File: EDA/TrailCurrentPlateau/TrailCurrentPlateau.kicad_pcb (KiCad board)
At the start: 2 copper layers, 56.4 x 64.2 mm, 12 parts, among them J1 DHT22, U1 Amazon Buck Converter, U2 ESP32-C6-Super-Mini, U3 SN65HVD230, U4 ZX-XH2.54-4PWT

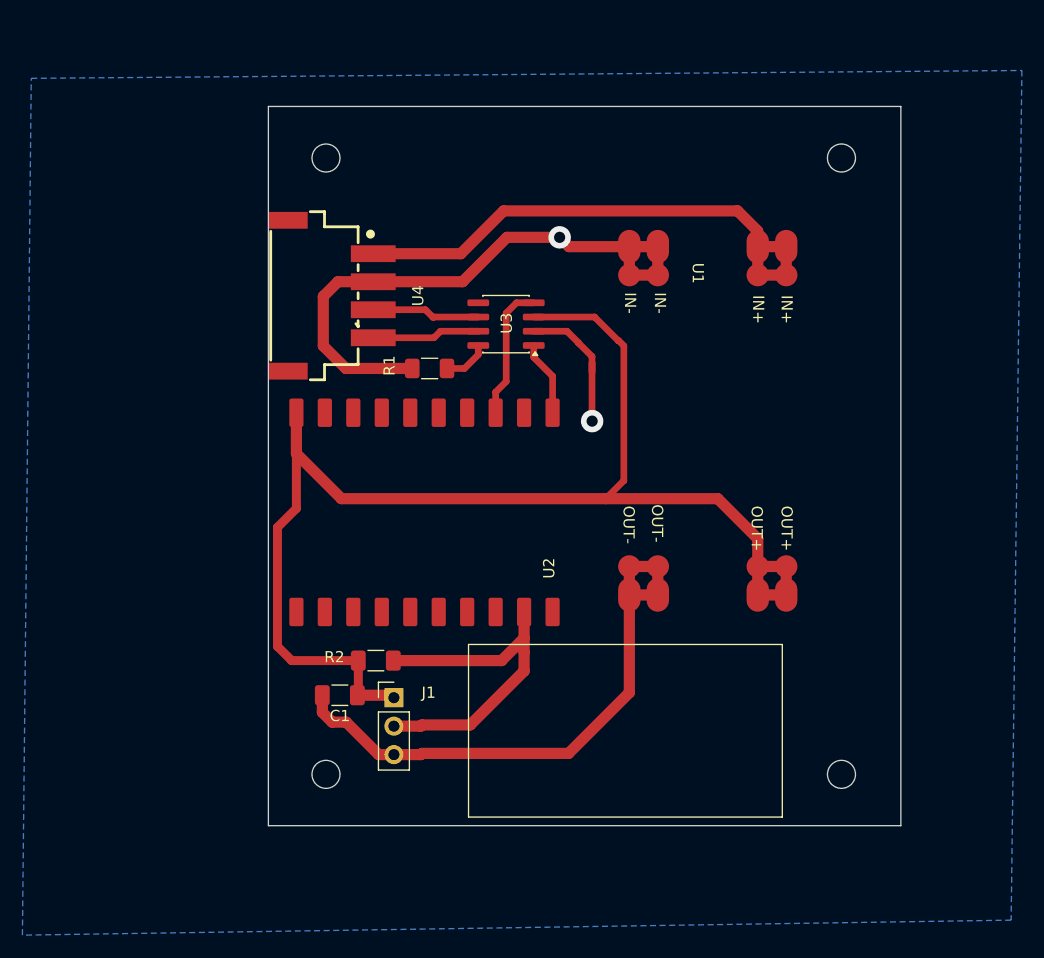
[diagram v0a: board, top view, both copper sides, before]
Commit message: Moved to ESP32S3 Zero board, adafruit bno055 and standard approach for CAN Bus and OTA
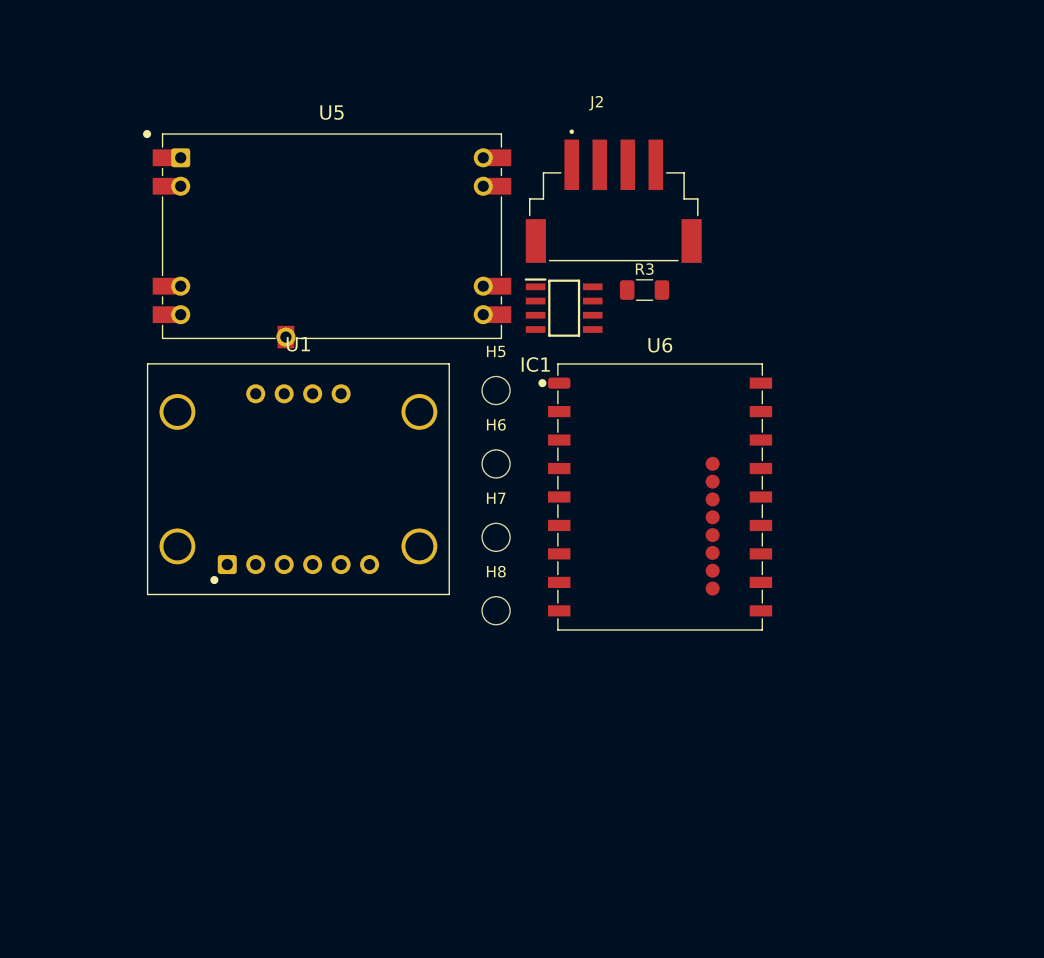
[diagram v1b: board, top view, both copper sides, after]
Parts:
- removed C1: 100nF, Capacitor_SMD:C_1206_3216Metric_Pad1.33x1.80mm_HandSolder
- removed H1, H2, H3, H4: MountingHole, MountingHole:MountingHole_2.5mm
- removed J1: DHT22, Connector_PinHeader_2.54mm:PinHeader_1x03_P2.54mm_Vertical
- removed R1: 10k, Resistor_SMD:R_1206_3216Metric_Pad1.30x1.75mm_HandSolder
- removed R2: 4.7K, Capacitor_SMD:C_1206_3216Metric_Pad1.33x1.80mm_HandSolder
- removed U2: ESP32-C6-Super-Mini, RF_Module:ESP32-C6-Super-Mini
- removed U3: SN65HVD230, Package_SO:SOIC-8_3.9x4.9mm_P1.27mm
- removed U4: ZX-XH2.54-4PWT, easyeda2kicad:CONN-SMD_4P-P2.50-WAFER-254W-4P
- added H5: MountingHole, MountingHole:MountingHole_2.5mm, F.Cu at (147.2, 85.8)
- added H6: MountingHole, MountingHole:MountingHole_2.5mm, F.Cu at (147.2, 92.3)
- added H7: MountingHole, MountingHole:MountingHole_2.5mm, F.Cu at (147.2, 98.8)
- added H8: MountingHole, MountingHole:MountingHole_2.5mm, F.Cu at (147.2, 105.4)
- added IC1: SN65HVD230DR, TrailCurrentFootprints:SN65HVD230DR, F.Cu at (153.3, 78.4)
- added J2: S4B-XH-SM4-TB, TrailCurrentFootprints:JST_S4B-XH-SM4-TB, F.Cu at (157.7, 72.4)
- added R3: 10k, Resistor_SMD:R_1206_3216Metric_Pad1.30x1.75mm_HandSolder, F.Cu at (160.4, 76.8)
- added U5: Mini560, TrailCurrentFootprints:Mini560, F.Cu at (132.5, 72.0)
- added U6: ESP32-S3-Zero, TrailCurrentFootprints:ESP32-S3-Zero_SMD, F.Cu at (161.8, 95.2)
- U1: value Amazon Buck Converter -> AdaFruit_BNO055; footprint Converter_DCDC:AmazonBuckConverter -> TrailCurrentFootprints:AdaFruit_BNO055
- moved U1 30.5 mm to (129.5, 93.7), turned to 0 degrees
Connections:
- U1 pad 1: +12V -> unconnected-(U1-VIN-Pad1)
- U1 pad 2: GND -> unconnected-(U1-3VO-Pad2)
- U1 pad 3: GND -> unconnected-(U1-GND-Pad3)
- U1 pad 4: +3.3V -> I2C_SDA
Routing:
- net GND: track 118.5 -> 0.00 mm, vias 2 -> 0
- net +3.3V: track 116.4 -> 0.00 mm
- net +12V: track 48.2 -> 0.00 mm
- net DHT_READING: track 32.7 -> 0.00 mm
- net CAN_RX: track 12.1 -> 0.00 mm
- net CANL: track 9.67 -> 0.00 mm
- net CANH: track 9.61 -> 0.00 mm
- net CAN_TX: track 6.70 -> 0.00 mm
- net Net-(U3-Rs): track 4.12 -> 0.00 mm
- removed copper zone on B.Cu, net GND
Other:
- board outline removed

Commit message: DIY EDA ready, CAM milling oeprations added
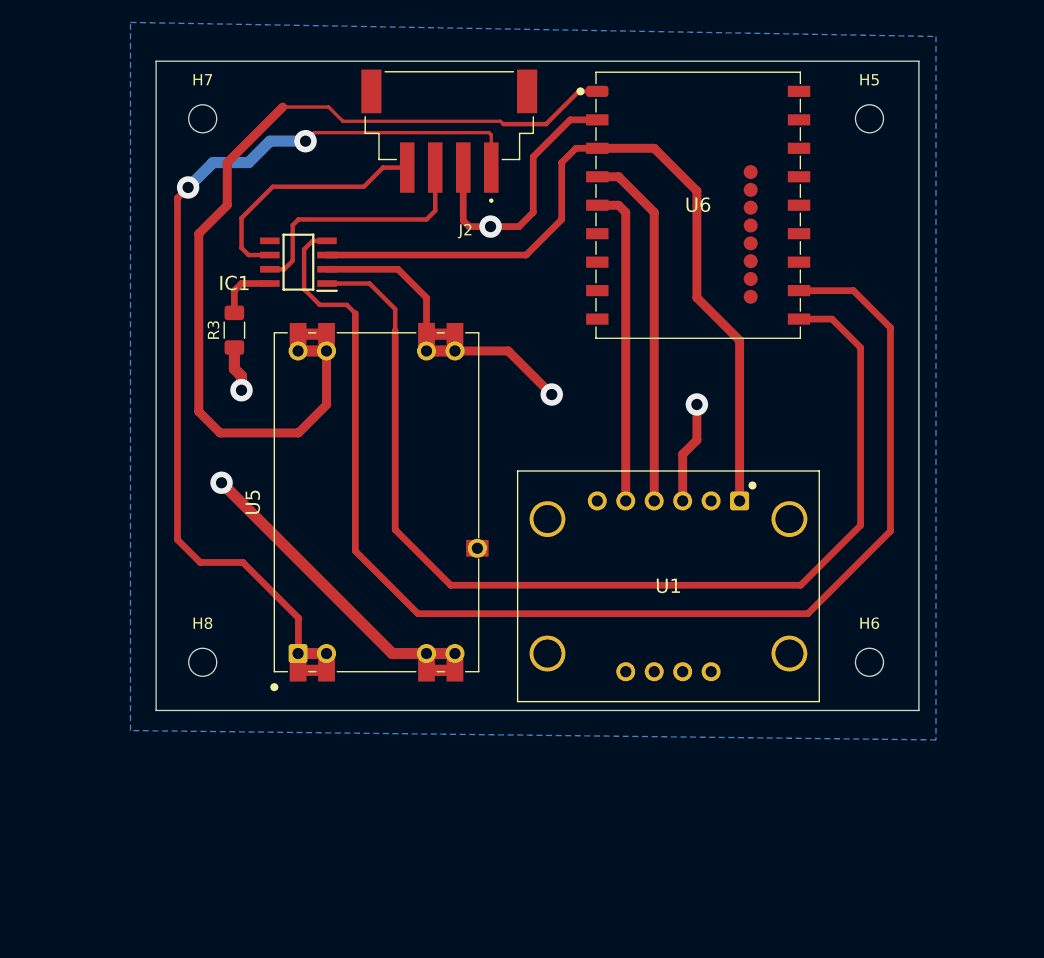
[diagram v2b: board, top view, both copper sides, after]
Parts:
- moved H7 45.6 mm to (121.0, 61.5)
- moved H5 41.2 mm to (180.5, 61.5)
- moved H6 37.7 mm to (180.5, 110.0)
- moved R3 36.8 mm to (123.8, 80.4), turned to 90 degrees
- moved U1 34.4 mm to (162.6, 103.2), turned to 180 degrees
- moved H8 26.6 mm to (121.0, 110.0)
- moved U6 26.3 mm to (165.2, 69.2)
- moved U5 24.1 mm to (136.5, 95.7), turned to 90 degrees
- moved IC1 24.1 mm to (129.5, 74.3), turned to 180 degrees
- moved J2 19.8 mm to (143.0, 59.1), turned to 180 degrees
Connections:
- U1 pad 1: unconnected-(U1-VIN-Pad1) -> +3.3V
- U1 pad 3: unconnected-(U1-GND-Pad3) -> GND
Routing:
- net CAN_RX: track 0.00 -> 113.4 mm
- net GND: track 0.00 -> 95.2 mm, vias 0 -> 5
- net CAN_TX: track 0.00 -> 94.9 mm
- net +12V: track 0.00 -> 87.4 mm, vias 0 -> 2
- net +5V: track 0.00 -> 83.3 mm
- net +3.3V: track 0.00 -> 70.7 mm
- net I2C_SDA: track 0.00 -> 32.1 mm
- net I2C_SCL: track 0.00 -> 28.6 mm
- net CANH: track 0.00 -> 22.6 mm
- net CANL: track 0.00 -> 22.1 mm
- net Net-(IC1-RS): track 0.00 -> 5.41 mm
- added copper zone on B.Cu, net GND
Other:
- board outline added: 68.1 x 57.9 mm

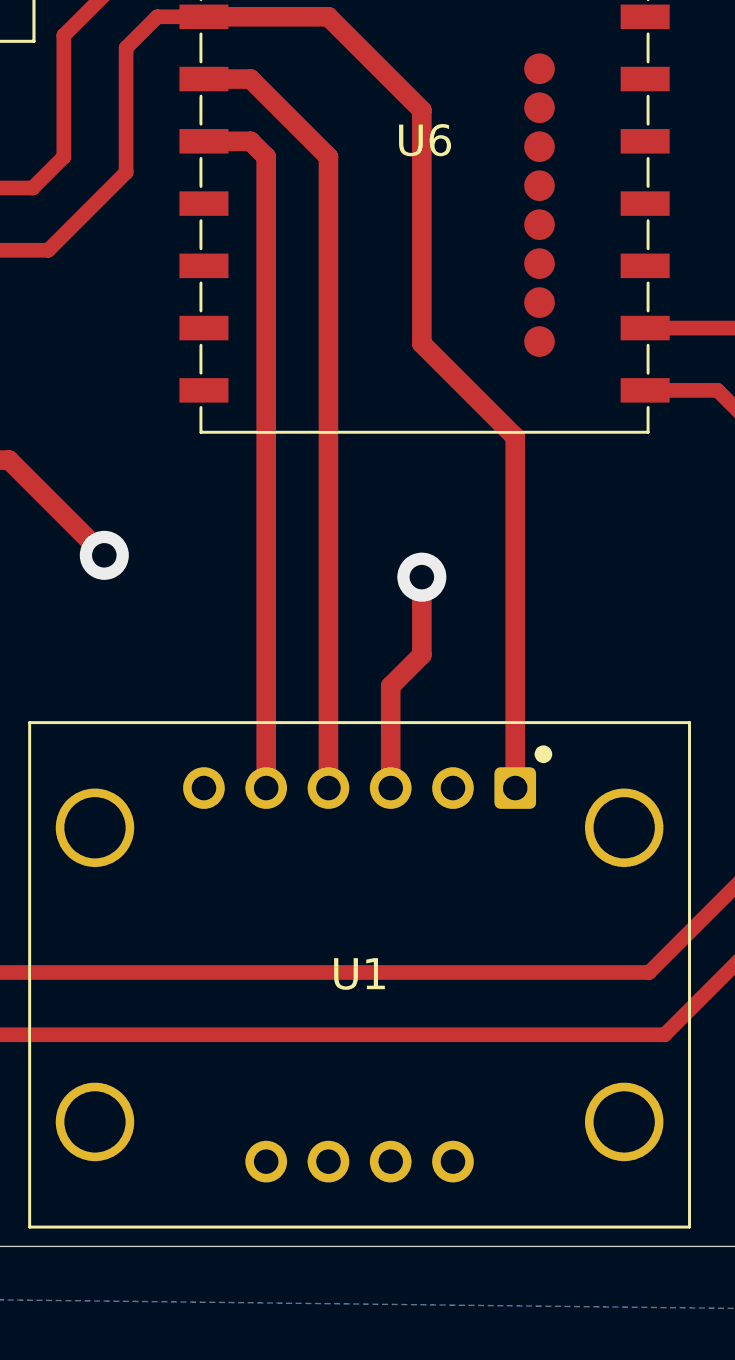
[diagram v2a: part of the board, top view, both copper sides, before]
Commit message: EDA Changes to fix Adafruit BNO055 older style footprint
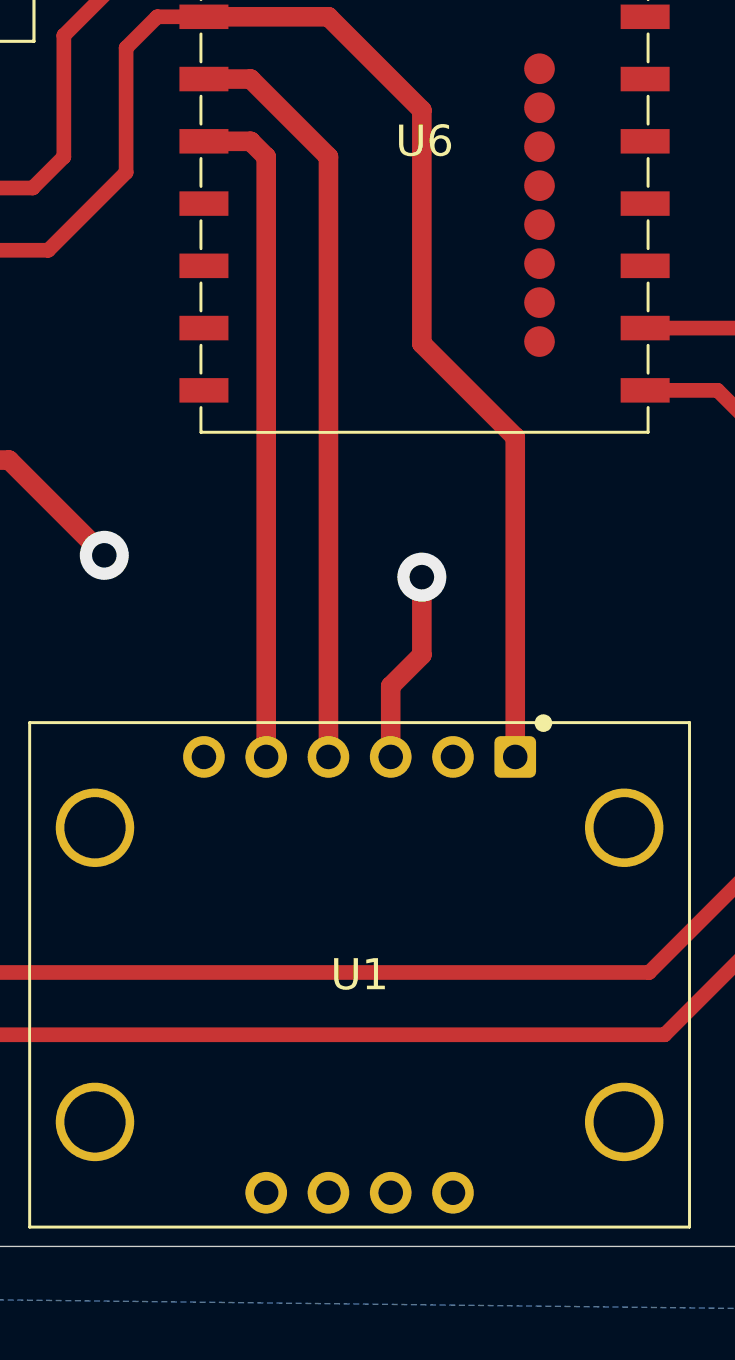
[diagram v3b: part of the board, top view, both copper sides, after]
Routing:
- net GND: track 95.2 -> 93.9 mm
- net +3.3V: track 70.7 -> 69.5 mm
- net I2C_SCL: track 28.6 -> 27.3 mm
- net I2C_SDA: track 32.1 -> 30.9 mm

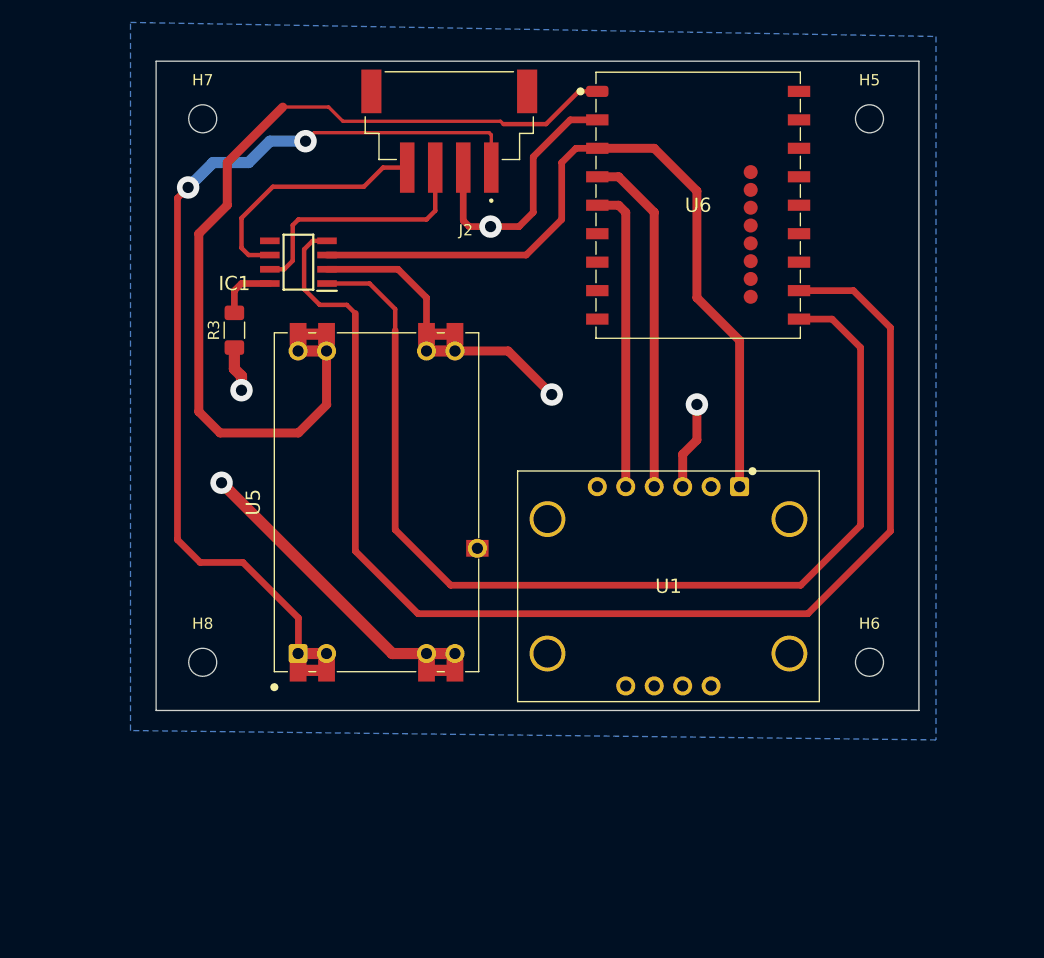
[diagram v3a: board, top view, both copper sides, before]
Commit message: Updates to improve the calibration process and communicate that to headwaters.
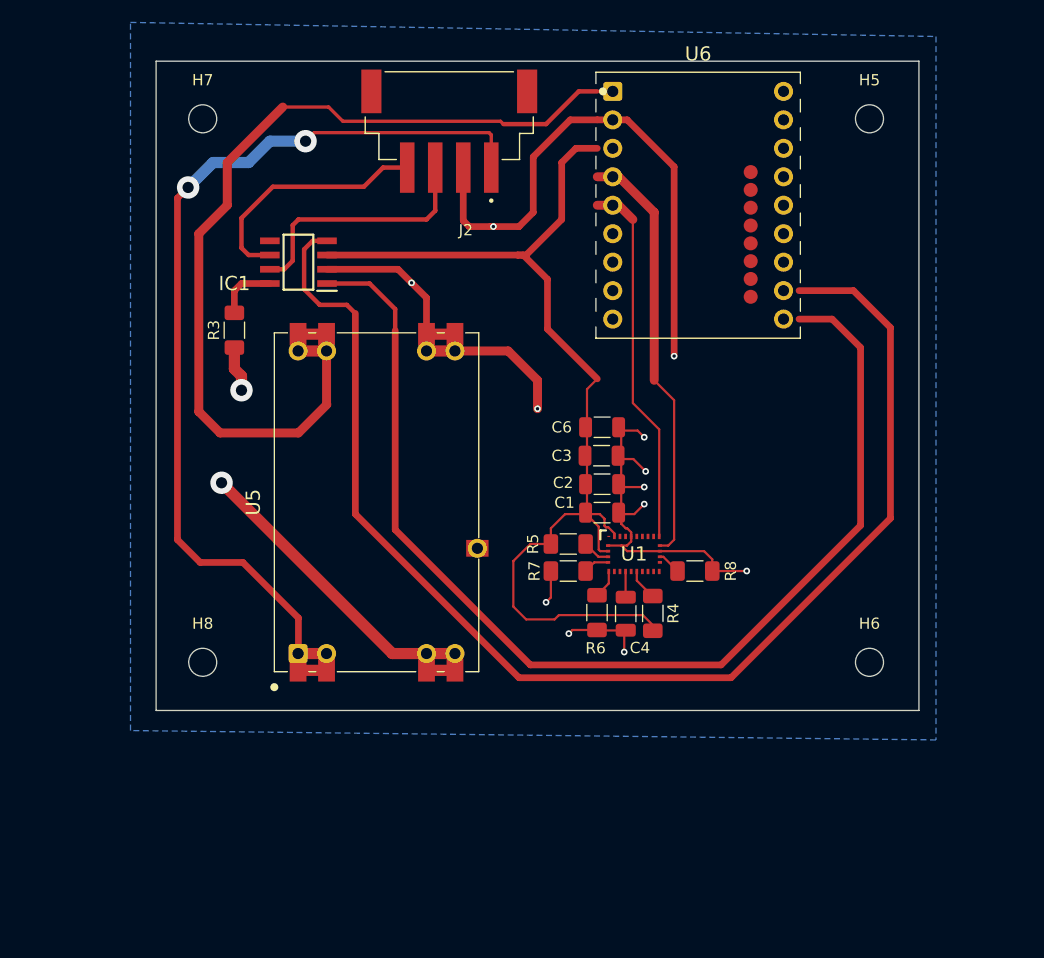
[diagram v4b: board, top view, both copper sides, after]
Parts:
- added C1: 1uF, Capacitor_SMD:C_1206_3216Metric, F.Cu at (156.6, 96.6)
- added C2: 100nF, Capacitor_SMD:C_1206_3216Metric, F.Cu at (156.6, 94.1)
- added C3: 100nF, Capacitor_SMD:C_1206_3216Metric, F.Cu at (156.6, 91.6)
- added C4: 1uF, Capacitor_SMD:C_1206_3216Metric, F.Cu at (158.8, 105.7)
- added C6: 10uF, Capacitor_SMD:C_1206_3216Metric, F.Cu at (156.6, 89.0)
- added R4: 10k, Resistor_SMD:R_1206_3216Metric_Pad1.30x1.75mm_HandSolder, F.Cu at (161.2, 105.6)
- added R5: 10k, Resistor_SMD:R_1206_3216Metric_Pad1.30x1.75mm_HandSolder, F.Cu at (153.6, 99.4)
- added R6: 10k, Resistor_SMD:R_1206_3216Metric_Pad1.30x1.75mm_HandSolder, F.Cu at (156.2, 105.6)
- added R7: 10k, Resistor_SMD:R_1206_3216Metric_Pad1.30x1.75mm_HandSolder, F.Cu at (153.6, 101.9)
- added R8: 10k, Resistor_SMD:R_1206_3216Metric_Pad1.30x1.75mm_HandSolder, F.Cu at (164.9, 101.9)
- U1: value AdaFruit_BNO055 -> BNO055; footprint TrailCurrentFootprints:AdaFruit_BNO055 -> TrailCurrentFootprints:BNO055_LGA-28_3.8x5.2mm
- U6: footprint TrailCurrentFootprints:ESP32-S3-Zero_SMD -> TrailCurrentFootprints:ESP32-S3-Zero_TH
- moved U1 4.22 mm to (159.5, 100.3), turned to 0 degrees
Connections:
- U1 pad 1: +3.3V -> unconnected-(U1-PIN1-Pad1)
- U1 pad 2: unconnected-(U1-3VO-Pad2) -> GND
- U1 pad 3: GND -> +3.3V
- U1 pad 4: I2C_SDA -> Net-(U1-nBOOT)
- U1 pad 5: I2C_SCL -> Net-(U1-PS1)
- U1 pad 6: unconnected-(U1-RST-Pad6) -> Net-(U1-PS0)
- U1 pad 9: unconnected-(U1-INT-Pad9) -> Net-(U1-CAP)
- U6 pad 4: I2C_SDA -> I2C_SCL
- U6 pad 5: I2C_SCL -> I2C_SDA
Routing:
- net GND: track 93.9 -> 156.8 mm, vias 5 -> 14
- net +3.3V: track 69.5 -> 93.3 mm
- net I2C_SCL: track 27.3 -> 37.8 mm
- net CAN_TX: track 94.9 -> 100.8 mm
- net Net-(U1-nRESET): track 0.00 -> 2.66 mm
- net Net-(U1-PS0): track 0.00 -> 2.56 mm
- net Net-(U1-nBOOT): track 0.00 -> 2.48 mm
- net Net-(U1-PS1): track 0.00 -> 2.33 mm
- net Net-(U1-CAP): track 0.00 -> 2.19 mm
- net CAN_RX: track 113.4 -> 115.5 mm
- net Net-(U1-COM3): track 0.00 -> 2.10 mm
- net I2C_SDA: track 30.9 -> 33.0 mm
